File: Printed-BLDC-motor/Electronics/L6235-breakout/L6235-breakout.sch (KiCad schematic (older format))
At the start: 35 parts, among them IC1 7805DT, J1 CONTROL, J2 HALL, J3 MOTOR, J5 PWR, U1 L6235PD

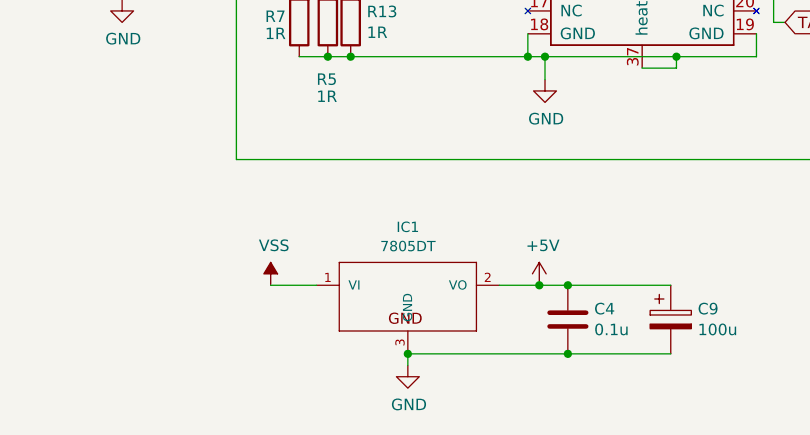
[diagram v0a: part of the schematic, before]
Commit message: Footprint of TO-220 7805 corrected.
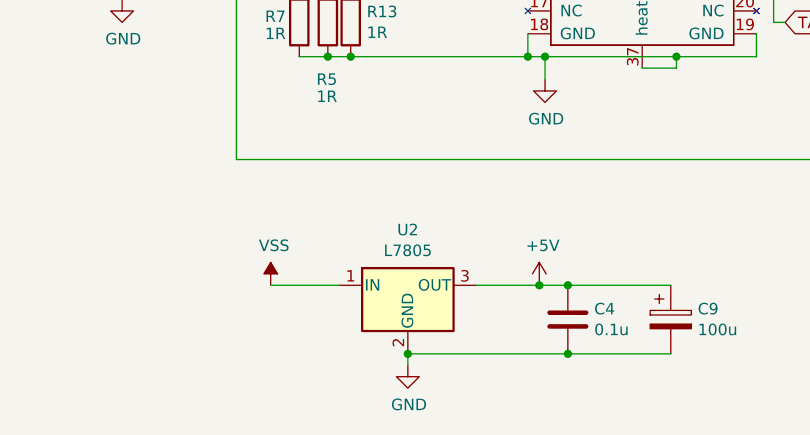
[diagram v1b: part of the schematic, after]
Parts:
- removed IC1: 7805DT, Package_TO_SOT_SMD:TO-252-2, symbol L6235-breakout-rescue:7805DT-adafruit-new
- added U2: L7805, Package_TO_SOT_SMD:TO-252-2, symbol Regulator_Linear:L7805
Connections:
- net +5V: now also U2.3 (OUT)
- net GND: now also U2.2 (GND)
- net VSS: now also U2.1 (IN)
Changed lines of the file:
@@
 	6800 3075 7150 3075
-$Comp
-L L6235-breakout-rescue:7805DT-adafruit-new IC1
-U 1 1 616EDC10
-P 5625 4075
-F 0 "IC1" H 5625 4329 45  0000 C CNN
-F 1 "7805DT" H 5625 4245 45  0000 C CNN
-F 2 "Package_TO_SOT_SMD:TO-252-2" H 5655 4225 20  0001 C CNN
-F 3 "" H 5625 4075 50  0001 C CNN
-	1    5625 4075
-	1    0    0    -1
-$EndComp
 $Comp
 L power:+5V #PWR0104
@@
 Wire Wire Line
 	2475 3800 2925 3800
-Wire Wire Line
-	5025 4075 5225 4075
 $Comp
 L power:GND #PWR0115
@@
 	5625 4375 5625 4425
 Wire Wire Line
-	6025 4075 6200 4075
-Wire Wire Line
 	6200 4075 6325 4075
 Connection ~ 6200 4075
@@
 	6325 4375 5625 4375
 Connection ~ 6325 4375
-Connection ~ 5625 4375
 $Comp
 L Mechanical:MountingHole H4
@@
 	1    0    0    -1
 $EndComp
+$Comp
+L Regulator_Linear:L7805 U2
+U 1 1 61E6127E
+P 5625 4075
+F 0 "U2" H 5625 4317 50  0000 C CNN
+F 1 "L7805" H 5625 4226 50  0000 C CNN
+F 2 "Package_TO_SOT_SMD:TO-252-2" H 5650 3925 50  0001 L CIN
+F 3 "http://www.st.com/content/ccc/resource/technical/document/datasheet/41/4f/b3/b0/12/d4/47/88/CD00000444.pdf/files/CD00000444.pdf/jcr:content/translations/en.CD00000444.pdf" H 5625 4025 50  0001 C CNN
+	1    5625 4075
+	1    0    0    -1
+$EndComp
+Connection ~ 5625 4375
+Wire Wire Line
+	5925 4075 6200 4075
+Wire Wire Line
+	5025 4075 5325 4075
 $EndSCHEMATC

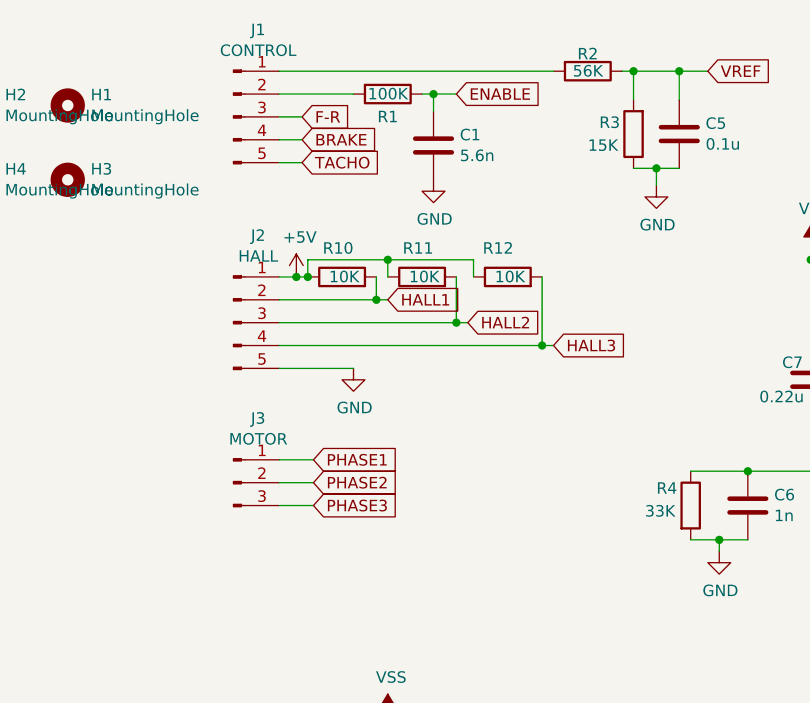
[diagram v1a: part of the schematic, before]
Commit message: Added ground reference to control connector.
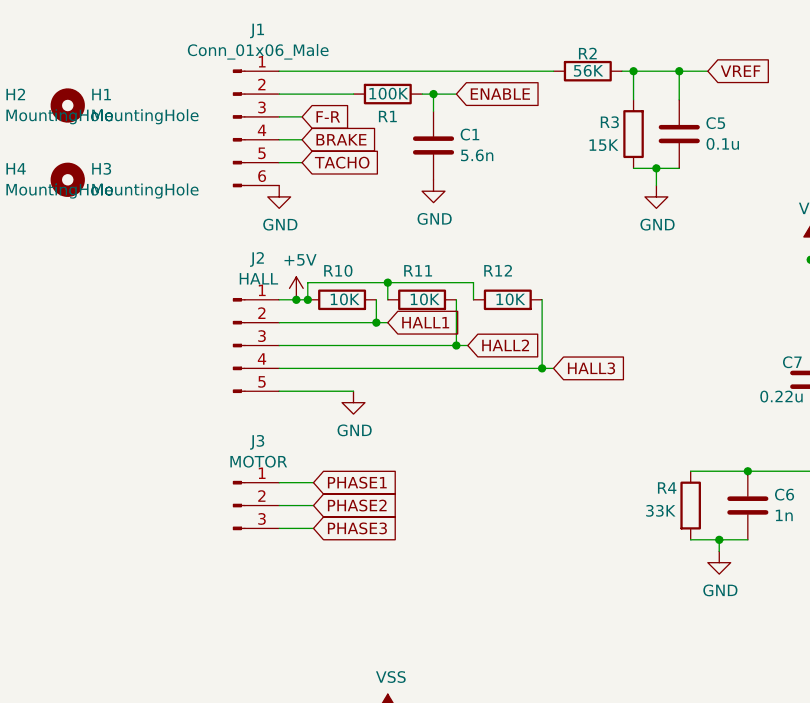
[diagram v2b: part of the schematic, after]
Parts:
- removed J1: CONTROL, Connector_PinHeader_2.54mm:PinHeader_1x05_P2.54mm_Vertical, symbol Connector:Conn_01x05_Male
- added J1: Conn_01x06_Male, Connector_PinHeader_2.54mm:PinHeader_1x06_P2.54mm_Vertical, symbol Connector:Conn_01x06_Male
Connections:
- net BRAKE: now also J1.4 (Pin_4)
- net F-R: now also J1.3 (Pin_3)
- net GND: now also J1.6 (Pin_6)
- net TACHO: now also J1.5 (Pin_5)
- net at R1.2: now also J1.2 (Pin_2)
- net at R2.2: now also J1.1 (Pin_1)
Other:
- moved on the sheet: J2, J3, R10, R11, R12
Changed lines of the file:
@@
 L Connector:Conn_01x03_Male J3
 U 1 1 615B4674
-P 2250 2525
-F 0 "J3" H 2358 2806 50  0000 C CNN
-F 1 "MOTOR" H 2358 2715 50  0000 C CNN
-F 2 "Connector_PinHeader_2.54mm:PinHeader_1x03_P2.54mm_Vertical" H 2250 2525 50  0001 C CNN
-F 3 "~" H 2250 2525 50  0001 C CNN
-	1    2250 2525
+P 2250 2625
+F 0 "J3" H 2358 2906 50  0000 C CNN
+F 1 "MOTOR" H 2358 2815 50  0000 C CNN
+F 2 "Connector_PinHeader_2.54mm:PinHeader_1x03_P2.54mm_Vertical" H 2250 2625 50  0001 C CNN
+F 3 "~" H 2250 2625 50  0001 C CNN
+	1    2250 2625
 	1    0    0    -1
 $EndComp
@@
 L Connector:Conn_01x05_Male J2
 U 1 1 615B5762
-P 2250 1825
-F 0 "J2" H 2358 2206 50  0000 C CNN
-F 1 "HALL" H 2358 2115 50  0000 C CNN
-F 2 "Connector_PinHeader_2.54mm:PinHeader_1x05_P2.54mm_Vertical" H 2250 1825 50  0001 C CNN
-F 3 "~" H 2250 1825 50  0001 C CNN
-	1    2250 1825
+P 2250 1925
+F 0 "J2" H 2358 2306 50  0000 C CNN
+F 1 "HALL" H 2358 2215 50  0000 C CNN
+F 2 "Connector_PinHeader_2.54mm:PinHeader_1x05_P2.54mm_Vertical" H 2250 1925 50  0001 C CNN
+F 3 "~" H 2250 1925 50  0001 C CNN
+	1    2250 1925
 	1    0    0    -1
 $EndComp
@@
 Wire Wire Line
 	2925 3800 2925 3875
+Text GLabel 2600 2725 2    50   Input ~ 0
+PHASE3
 Text GLabel 2600 2625 2    50   Input ~ 0
-PHASE3
+PHASE2
 Text GLabel 2600 2525 2    50   Input ~ 0
-PHASE2
-Text GLabel 2600 2425 2    50   Input ~ 0
 PHASE1
 Wire Wire Line
+	2600 2725 2450 2725
+Wire Wire Line
 	2600 2625 2450 2625
 Wire Wire Line
 	2600 2525 2450 2525
-Wire Wire Line
-	2600 2425 2450 2425
 $Comp
 L power:GND #PWR0105
 U 1 1 615CBCF5
-P 2775 2025
-F 0 "#PWR0105" H 2775 1775 50  0001 C CNN
-F 1 "GND" H 2780 1852 50  0000 C CNN
-F 2 "" H 2775 2025 50  0001 C CNN
-F 3 "" H 2775 2025 50  0001 C CNN
-	1    2775 2025
+P 2775 2125
+F 0 "#PWR0105" H 2775 1875 50  0001 C CNN
+F 1 "GND" H 2780 1952 50  0000 C CNN
+F 2 "" H 2775 2125 50  0001 C CNN
+F 3 "" H 2775 2125 50  0001 C CNN
+	1    2775 2125
 	1    0    0    -1
 $EndComp
@@
 L power:+5V #PWR0106
 U 1 1 615CC61D
-P 2525 1625
-F 0 "#PWR0106" H 2525 1475 50  0001 C CNN
-F 1 "+5V" H 2540 1798 50  0000 C CNN
-F 2 "" H 2525 1625 50  0001 C CNN
-F 3 "" H 2525 1625 50  0001 C CNN
-	1    2525 1625
-	1    0    0    -1
-$EndComp
-Wire Wire Line
-	2450 2025 2775 2025
-Wire Wire Line
-	2450 1625 2525 1625
-Text GLabel 3650 1925 2    50   Input ~ 0
+P 2525 1725
+F 0 "#PWR0106" H 2525 1575 50  0001 C CNN
+F 1 "+5V" H 2540 1898 50  0000 C CNN
+F 2 "" H 2525 1725 50  0001 C CNN
+F 3 "" H 2525 1725 50  0001 C CNN
+	1    2525 1725
+	1    0    0    -1
+$EndComp
+Wire Wire Line
+	2450 2125 2775 2125
+Wire Wire Line
+	2450 1725 2525 1725
+Text GLabel 3650 2025 2    50   Input ~ 0
 HALL3
-Text GLabel 3275 1825 2    50   Input ~ 0
+Text GLabel 3275 1925 2    50   Input ~ 0
 HALL2
-Text GLabel 2925 1725 2    50   Input ~ 0
+Text GLabel 2925 1825 2    50   Input ~ 0
 HALL1
 Text GLabel 2550 1025 2    50   Input ~ 0
@@
 L Device:R R10
 U 1 1 61701AD2
-P 2725 1625
-F 0 "R10" V 2850 1575 50  0000 L CNN
-F 1 "10K" V 2725 1550 50  0000 L CNN
-F 2 "Resistor_SMD:R_0805_2012Metric" V 2655 1625 50  0001 C CNN
-F 3 "~" H 2725 1625 50  0001 C CNN
-	1    2725 1625
+P 2725 1725
+F 0 "R10" V 2850 1675 50  0000 L CNN
+F 1 "10K" V 2725 1650 50  0000 L CNN
+F 2 "Resistor_SMD:R_0805_2012Metric" V 2655 1725 50  0001 C CNN
+F 3 "~" H 2725 1725 50  0001 C CNN
+	1    2725 1725
 	0    -1   -1   0
 $EndComp
 Wire Wire Line
-	2875 1725 2875 1625
-Wire Wire Line
-	2450 1725 2875 1725
-Wire Wire Line
-	2575 1625 2525 1625
-Connection ~ 2525 1625
+	2875 1825 2875 1725
+Wire Wire Line
+	2450 1825 2875 1825
+Wire Wire Line
+	2575 1725 2525 1725
+Connection ~ 2525 1725
 $Comp
 L Device:R R11
 U 1 1 617501EE
-P 3075 1625
-F 0 "R11" V 3200 1575 50  0000 L CNN
-F 1 "10K" V 3075 1550 50  0000 L CNN
-F 2 "Resistor_SMD:R_0805_2012Metric" V 3005 1625 50  0001 C CNN
-F 3 "~" H 3075 1625 50  0001 C CNN
-	1    3075 1625
+P 3075 1725
+F 0 "R11" V 3200 1675 50  0000 L CNN
+F 1 "10K" V 3075 1650 50  0000 L CNN
+F 2 "Resistor_SMD:R_0805_2012Metric" V 3005 1725 50  0001 C CNN
+F 3 "~" H 3075 1725 50  0001 C CNN
+	1    3075 1725
 	0    -1   -1   0
 $EndComp
@@
 L Device:R R12
 U 1 1 617506DC
-P 3450 1625
-F 0 "R12" V 3575 1600 50  0000 L CNN
-F 1 "10K" V 3450 1550 50  0000 L CNN
-F 2 "Resistor_SMD:R_0805_2012Metric" V 3380 1625 50  0001 C CNN
-F 3 "~" H 3450 1625 50  0001 C CNN
-	1    3450 1625
+P 3450 1725
+F 0 "R12" V 3575 1700 50  0000 L CNN
+F 1 "10K" V 3450 1650 50  0000 L CNN
+F 2 "Resistor_SMD:R_0805_2012Metric" V 3380 1725 50  0001 C CNN
+F 3 "~" H 3450 1725 50  0001 C CNN
+	1    3450 1725
 	0    -1   -1   0
 $EndComp
 Wire Wire Line
-	2575 1625 2575 1550
-Wire Wire Line
-	2575 1550 2925 1550
-Wire Wire Line
-	2925 1550 2925 1625
-Connection ~ 2575 1625
-Wire Wire Line
-	2925 1550 3300 1550
-Wire Wire Line
-	3300 1550 3300 1625
-Connection ~ 2925 1550
-Wire Wire Line
-	3225 1825 3225 1625
-Wire Wire Line
-	2450 1825 3225 1825
-Wire Wire Line
-	3600 1925 3600 1625
-Wire Wire Line
-	2450 1925 3600 1925
-Wire Wire Line
-	2925 1725 2875 1725
-Connection ~ 2875 1725
-Wire Wire Line
-	3225 1825 3275 1825
-Connection ~ 3225 1825
-Wire Wire Line
-	3650 1925 3600 1925
-Connection ~ 3600 1925
-$Comp
-L Connector:Conn_01x05_Male J1
-U 1 1 6177BB55
-P 2250 925
-F 0 "J1" H 2358 1306 50  0000 C CNN
-F 1 "CONTROL" H 2358 1215 50  0000 C CNN
-F 2 "Connector_PinHeader_2.54mm:PinHeader_1x05_P2.54mm_Vertical" H 2250 925 50  0001 C CNN
-F 3 "~" H 2250 925 50  0001 C CNN
-	1    2250 925
-	1    0    0    -1
-$EndComp
+	2575 1725 2575 1650
+Wire Wire Line
+	2575 1650 2925 1650
+Wire Wire Line
+	2925 1650 2925 1725
+Connection ~ 2575 1725
+Wire Wire Line
+	2925 1650 3300 1650
+Wire Wire Line
+	3300 1650 3300 1725
+Connection ~ 2925 1650
+Wire Wire Line
+	3225 1925 3225 1725
+Wire Wire Line
+	2450 1925 3225 1925
+Wire Wire Line
+	3600 2025 3600 1725
+Wire Wire Line
+	2450 2025 3600 2025
+Wire Wire Line
+	2925 1825 2875 1825
+Connection ~ 2875 1825
+Wire Wire Line
+	3225 1925 3275 1925
+Connection ~ 3225 1925
+Wire Wire Line
+	3650 2025 3600 2025
+Connection ~ 3600 2025
 Text GLabel 2550 1125 2    50   Input ~ 0
 TACHO
@@
 Wire Wire Line
 	5025 4075 5325 4075
+$Comp
+L Connector:Conn_01x06_Male J1
+U 1 1 61E8B4F3
+P 2250 925
+F 0 "J1" H 2358 1306 50  0000 C CNN
+F 1 "Conn_01x06_Male" H 2358 1215 50  0000 C CNN
+F 2 "Connector_PinHeader_2.54mm:PinHeader_1x06_P2.54mm_Vertical" H 2250 925 50  0001 C CNN
+F 3 "~" H 2250 925 50  0001 C CNN
+	1    2250 925
+	1    0    0    -1
+$EndComp
+$Comp
+L power:GND #PWR0116
+U 1 1 61E9687C
+P 2450 1225
+F 0 "#PWR0116" H 2450 975 50  0001 C CNN
+F 1 "GND" H 2455 1052 50  0000 C CNN
+F 2 "" H 2450 1225 50  0001 C CNN
+F 3 "" H 2450 1225 50  0001 C CNN
+	1    2450 1225
+	1    0    0    -1
+$EndComp
 $EndSCHEMATC

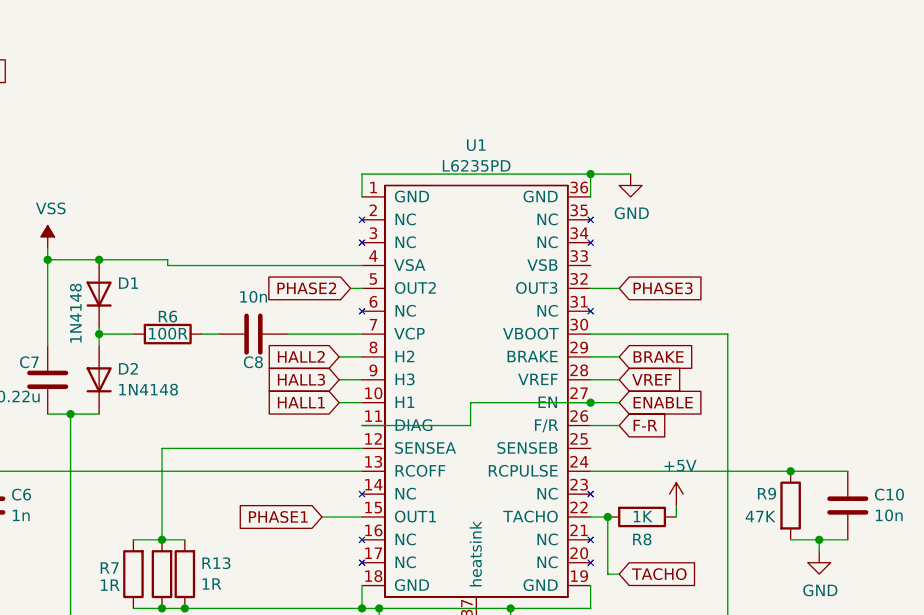
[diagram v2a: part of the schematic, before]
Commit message: Fixed missing chip connetions.
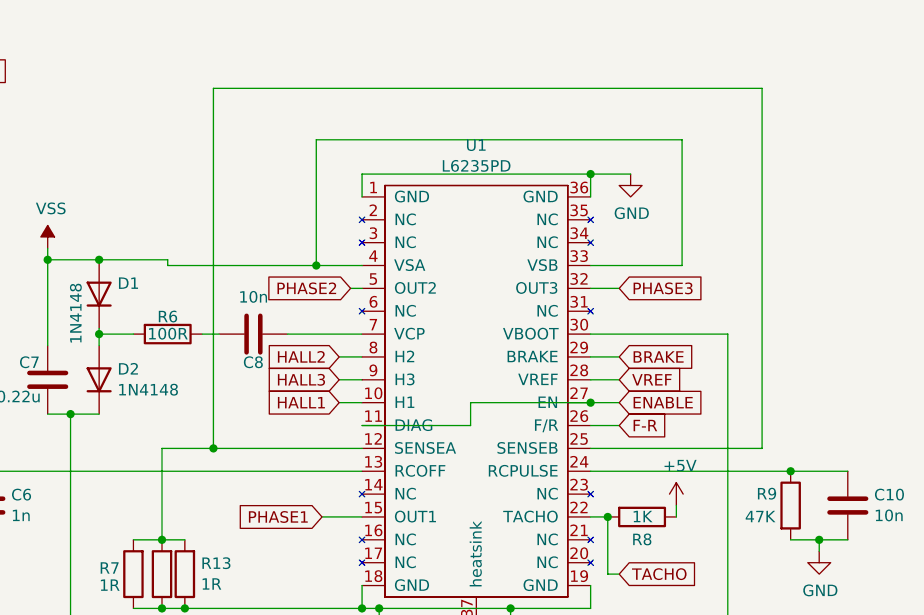
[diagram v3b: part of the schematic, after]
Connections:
- net VSS: now also U1.33 (VSB)
- net at R13.2, R5.2, R7.2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: now also U1.25 (SENSEB)
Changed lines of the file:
@@
 $EndComp
 Wire Wire Line
-	5275 2375 6150 2375
+	5275 2375 5500 2375
 Wire Wire Line
 	6625 2175 7150 2175
 Wire Wire Line
-	5300 1575 6150 1575
+	5300 1575 5950 1575
 Connection ~ 7150 2175
 Wire Wire Line
@@
 	1    0    0    -1
 $EndComp
+Wire Wire Line
+	7150 1575 7550 1575
+Wire Wire Line
+	7550 1575 7550 1025
+Wire Wire Line
+	7550 1025 5950 1025
+Wire Wire Line
+	5950 1025 5950 1575
+Connection ~ 5950 1575
+Wire Wire Line
+	5950 1575 6150 1575
+Wire Wire Line
+	7150 2375 7900 2375
+Wire Wire Line
+	7900 2375 7900 800
+Wire Wire Line
+	7900 800  5500 800
+Wire Wire Line
+	5500 800  5500 2375
+Connection ~ 5500 2375
+Wire Wire Line
+	5500 2375 6150 2375
 $EndSCHEMATC

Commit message: V2 PCB send for trial production.
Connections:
- net VSS renamed VDD
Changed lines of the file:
@@
-$EndComp
-$Comp
-L power:VSS #PWR0102
-U 1 1 615C52DE
-P 2925 3550
-F 0 "#PWR0102" H 2925 3400 50  0001 C CNN
-F 1 "VSS" H 2940 3723 50  0000 C CNN
-F 2 "" H 2925 3550 50  0001 C CNN
-F 3 "" H 2925 3550 50  0001 C CNN
-	1    2925 3550
-	1    0    0    -1
 $EndComp
 $Comp
@@
 Wire Wire Line
 	3125 3575 2925 3575
-Connection ~ 2925 3575
-Wire Wire Line
-	2925 3575 2925 3550
 Wire Wire Line
 	3125 3875 2925 3875
@@
 Wire Wire Line
 	5000 1550 4775 1550
-Wire Wire Line
-	4775 1550 4775 1925
 $Comp
 L Device:C C8
@@
 	5825 1875 6150 1875
 $Comp
-L power:VSS #PWR0108
-U 1 1 61611806
-P 4775 1500
-F 0 "#PWR0108" H 4775 1350 50  0001 C CNN
-F 1 "VSS" H 4790 1673 50  0000 C CNN
-F 2 "" H 4775 1500 50  0001 C CNN
-F 3 "" H 4775 1500 50  0001 C CNN
-	1    4775 1500
-	1    0    0    -1
-$EndComp
-Wire Wire Line
-	4775 1550 4775 1500
-Connection ~ 4775 1550
-$Comp
 L Device:R R5
 U 1 1 61613E1F
@@
 $EndComp
 $Comp
-L power:VSS #PWR0107
-U 1 1 616F094C
-P 5025 4075
-F 0 "#PWR0107" H 5025 3925 50  0001 C CNN
-F 1 "VSS" H 5040 4248 50  0000 C CNN
-F 2 "" H 5025 4075 50  0001 C CNN
-F 3 "" H 5025 4075 50  0001 C CNN
-	1    5025 4075
-	1    0    0    -1
-$EndComp
-$Comp
 L Device:CP C9
 U 1 1 616F1027
@@
 Wire Wire Line
 	5500 2375 6150 2375
+$Comp
+L power:VDD #PWR?
+U 1 1 61EB6368
+P 2925 3575
+F 0 "#PWR?" H 2925 3425 50  0001 C CNN
+F 1 "VDD" H 2940 3748 50  0000 C CNN
+F 2 "" H 2925 3575 50  0001 C CNN
+F 3 "" H 2925 3575 50  0001 C CNN
+	1    2925 3575
+	1    0    0    -1
+$EndComp
+Connection ~ 2925 3575
+$Comp
+L power:VDD #PWR?
+U 1 1 61EC379F
+P 4775 1500
+F 0 "#PWR?" H 4775 1350 50  0001 C CNN
+F 1 "VDD" H 4790 1673 50  0000 C CNN
+F 2 "" H 4775 1500 50  0001 C CNN
+F 3 "" H 4775 1500 50  0001 C CNN
+	1    4775 1500
+	1    0    0    -1
+$EndComp
+Wire Wire Line
+	4775 1550 4775 1500
+Wire Wire Line
+	4775 1550 4775 1925
+Connection ~ 4775 1550
+$Comp
+L power:VDD #PWR?
+U 1 1 61ED414A
+P 5025 4075
+F 0 "#PWR?" H 5025 3925 50  0001 C CNN
+F 1 "VDD" H 5040 4248 50  0000 C CNN
+F 2 "" H 5025 4075 50  0001 C CNN
+F 3 "" H 5025 4075 50  0001 C CNN
+	1    5025 4075
+	1    0    0    -1
+$EndComp
 $EndSCHEMATC
